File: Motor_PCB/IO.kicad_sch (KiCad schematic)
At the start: 54 parts, among them Q401 BC846, Q402 TPH4R50ANH1, Q403 TPH4R50ANH1, Q404 2N7002, Q405 2N7002, Q406 BC856, U401 VOM1271T, U402 TCAN1043xDxQ1

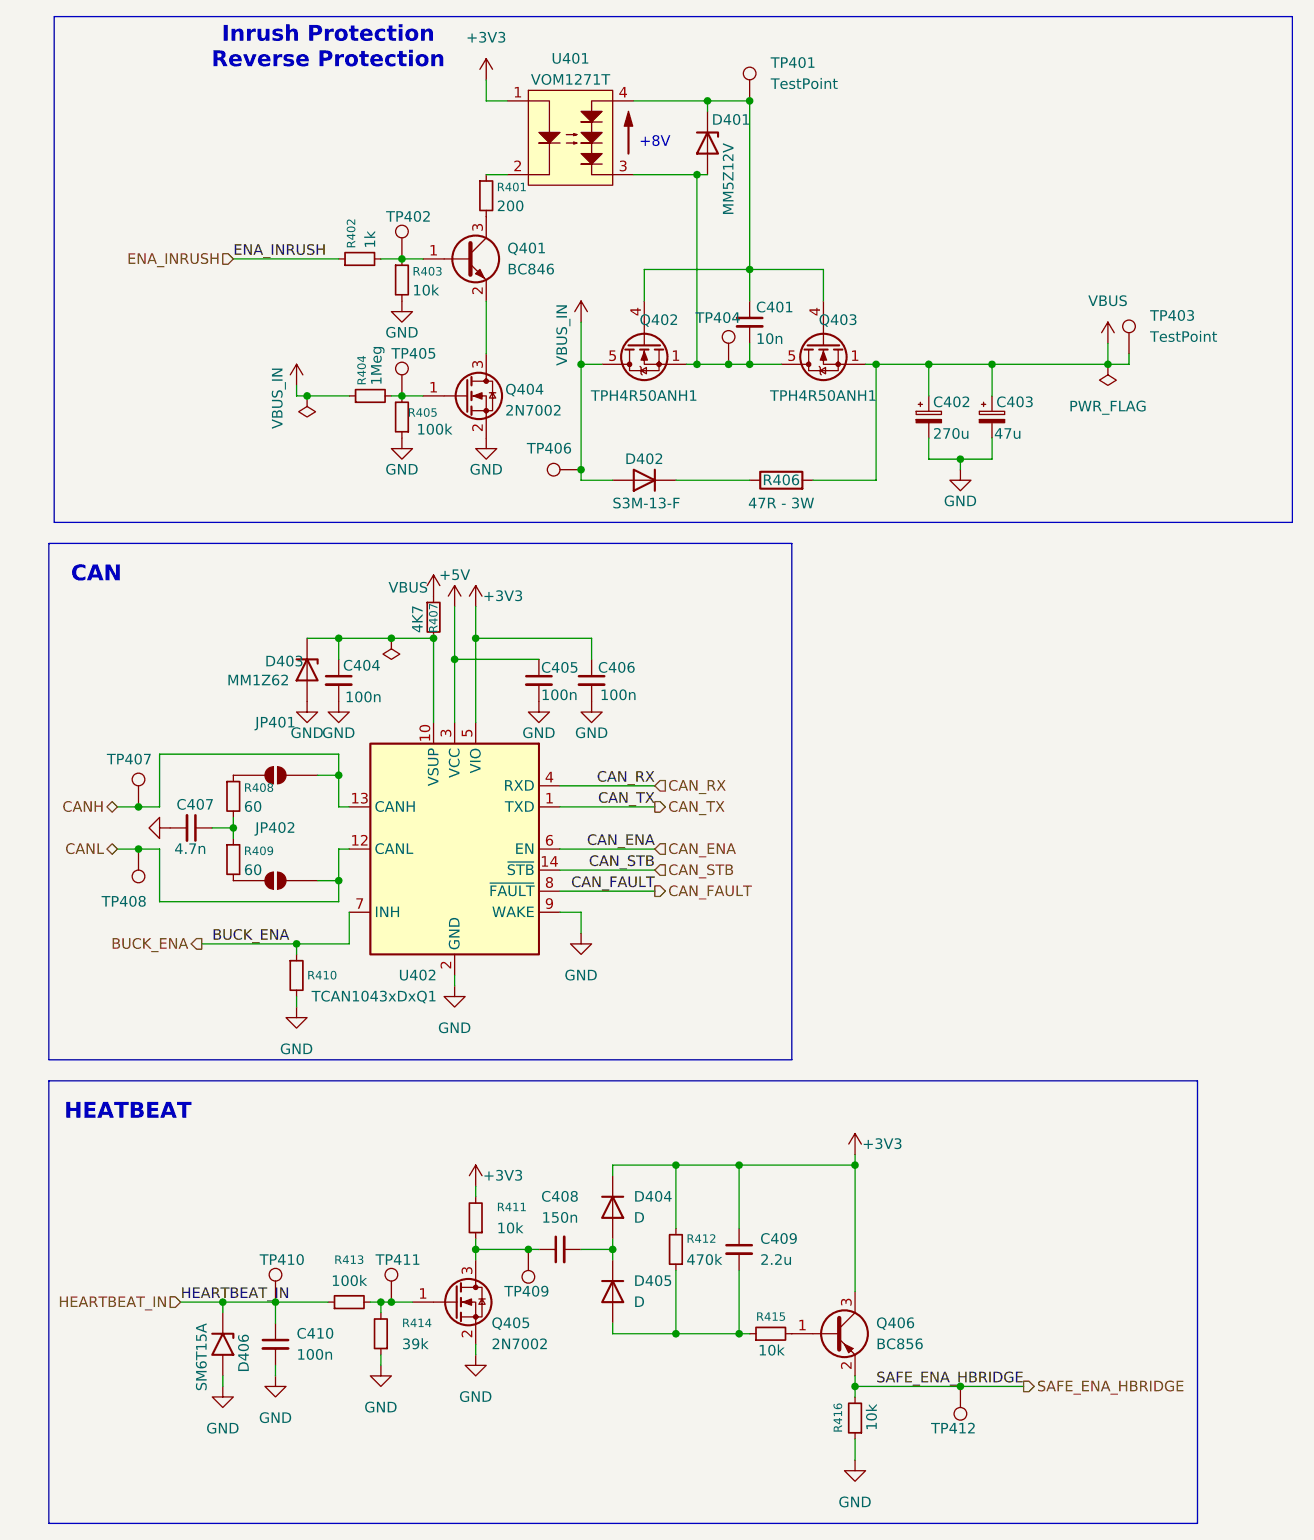
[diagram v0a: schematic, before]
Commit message: Fixed some Schematic mistakes
- Fixed mirroers FETS
- Added voltage divider to TCAN INH
- fixed other minor mistakes
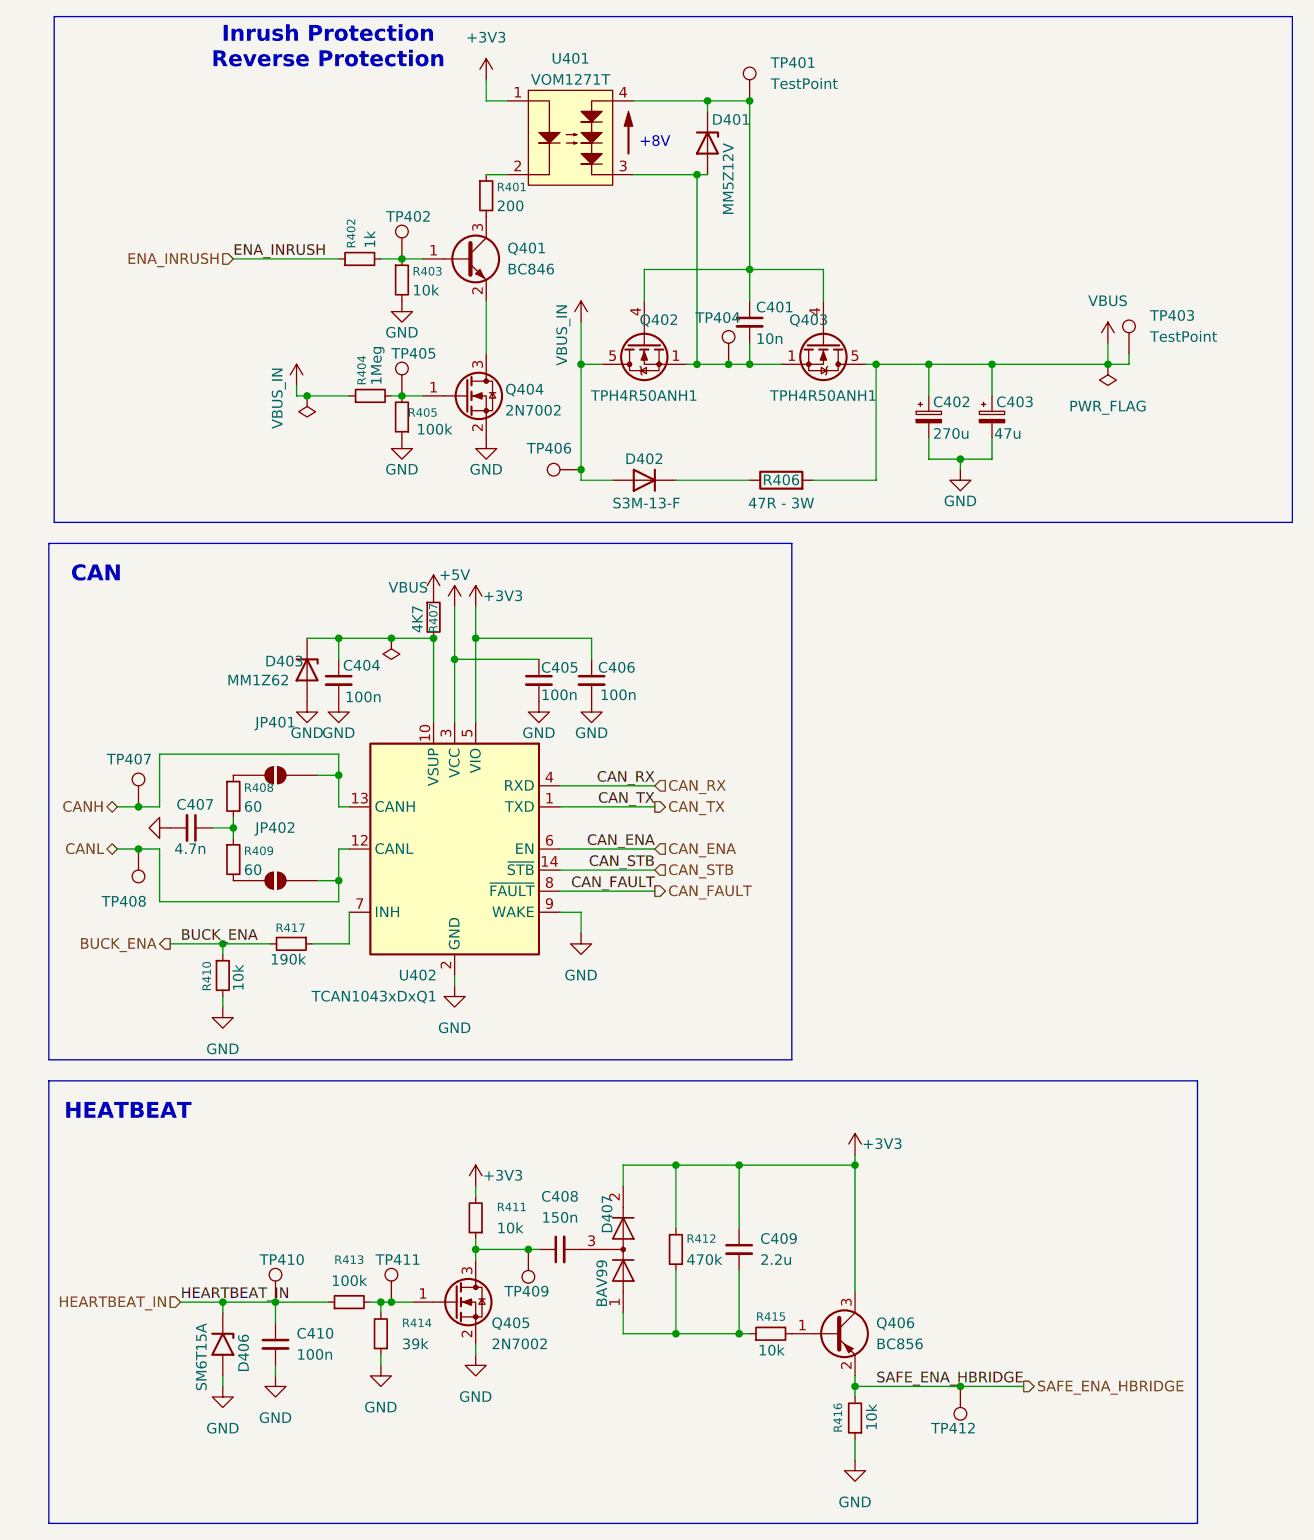
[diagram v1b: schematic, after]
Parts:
- removed D404, D405: D, Package_TO_SOT_SMD:SOT-23, symbol Device:D
- added D407: BAV99, Package_TO_SOT_SMD:SOT-23, symbol Diode:BAV99
- added R417: 190k, Resistor_SMD:R_0603_1608Metric, symbol Device:R_Small
- C408, C409, C410: footprint Diode_SMD:D_SMB -> Capacitor_SMD:C_0603_1608Metric
- D402: footprint Diode_SMD:D_SOD-323 -> Diode_SMD:D_SMC
- D403: footprint Diode_SMD:Littelfuse_PolyZen-LS -> Diode_SMD:D_SOD-123
- R407, R411, R412, R413, R414, R415, R416: footprint Resistor_THT:R_Array_SIP4 -> Resistor_SMD:R_0603_1608Metric
- R410: value 60 -> 10k
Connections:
- net +3V3: now also D407.2 (A)
- net BUCK_ENA: now also R417.2; no longer U402.7 (INH)
- net VBUS: now also Q403.5 (D); no longer Q403.1 (S), Q403.2 (S), Q403.3 (S)
- net at C409.2, R412.1, R415.1: now also D407.1 (K)
- net at C401.2, D401.2 (A), Q402.1 (S)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: now also Q403.1 (S), Q403.2 (S), Q403.3 (S); no longer Q403.5 (D)
- net at C408.2: now also D407.3 (K)
- new net: R417.1, U402.7 (INH)
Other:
- moved on the sheet: Q403, R410

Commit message: Surely i didnt miss anything else on the schematc...
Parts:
- R413: value 100k -> 50k
- R414: value 39k -> 100k
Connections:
- net +3V3: now also Q406.2 (E); no longer Q406.3 (C)
- net SAFE_ENA_HBRIDGE: now also Q406.3 (C); no longer Q406.2 (E)
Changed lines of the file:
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@@
 		(lib_id "Transistor_BJT:BC856")
 		(at 111.76 172.72 0)
+		(mirror x)
 		(unit 1)
 		(body_style 1)
@@
 		(in_pos_files yes)
 		(dnp no)
-		(fields_autoplaced yes)
 		(property "Reference" "Q406"
-			(at 116.84 171.4499 0)
+			(at 116.84 173.9901 0)
 			(show_name no)
 			(do_not_autoplace no)
@@
 		)
 		(property "Value" "BC856"
-			(at 116.84 173.9899 0)
+			(at 116.84 171.4501 0)
 			(show_name no)
 			(do_not_autoplace no)
@@
 		)
 		(property "Footprint" "Package_TO_SOT_SMD:SOT-23"
-			(at 116.84 174.625 0)
+			(at 116.84 170.815 0)
 			(hide yes)
 			(show_name no)
@@
 			)
 		)
-		(property "Value" "100k"
+		(property "Value" "50k"
 			(at 53.34 166.37 90)
 			(show_name no)
@@
 			)
 		)
-		(property "Value" "39k"
+		(property "Value" "100k"
 			(at 59.69 173.9899 0)
 			(show_name no)

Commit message: Updated schematic started on layout for motor PCB
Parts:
- removed TP407, TP408: TestPoint, TestPoint:TestPoint_Pad_D1.5mm, symbol Connector:TestPoint
- added C411: 100u, Capacitor_SMD:CP_Elec_10x10, symbol Device:C_Polarized_Small
- added D404: ESD2CANFD60-Q1, Package_TO_SOT_SMD:SOT-23-3, symbol Device:D_TVS_Dual_AAC
- C402: value 270u -> 100u; footprint Capacitor_SMD:CP_Elec_8x10.5 -> Capacitor_SMD:CP_Elec_10x10
- C403: value 47u -> 100u; footprint Capacitor_SMD:CP_Elec_8x10.5 -> Capacitor_SMD:CP_Elec_10x10
- U401: footprint Package_SO:SOP-4_7.5x4.1mm_P2.54mm -> MOTOR_PCB:SOP-4_VIS
- U402: value TCAN1043xDxQ1 -> TCAN1043H
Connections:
- net CANH: now also D404.2 (A2)
- net CANL: now also D404.1 (A1)
- net GND: now also C411.2, D404.3 (common)
- net VBUS: now also C411.1
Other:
- moved on the sheet: C404, C405, C406, C407, D403, JP401, JP402, R407, R408, R409, R410, R417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

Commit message: 20/10-2026
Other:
- moved on the sheet: C401, C402, C403, C404, C405, C406, C407, C408, C409, C410, C411, D401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

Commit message: 23-10-2026
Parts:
- Q404: value 2N7002 -> AO3400A; symbol Transistor_FET:2N7002 -> Transistor_FET:AO3400A
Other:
- note added: "Look at layout on CBT1 (placement, GND, distance from mcu and connector)"
- note added: "Reverse voltage of diode"
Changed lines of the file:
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@@
+		)
+	)
+	(text "Reverse voltage of diode"
+		(exclude_from_sim no)
+		(at 83.82 73.66 0)
+		(effects
+			(font
+				(size 1.27 1.27)
+			)
 		)
 	)
@@
 		)
 	)
+	(text "Look at layout on CBT1\n(placement, GND, distance from mcu and connector)"
+		(exclude_from_sim no)
+		(at 74.93 102.87 0)
+		(effects
+			(font
+				(size 1.27 1.27)
+			)
+		)
+	)
 	(text "CAN"
 		(exclude_from_sim no)
@@
 	(text "Inrush Protection\nReverse Protection"
 		(exclude_from_sim no)
-		(at 48.26 17.78 0)
+		(at 31.75 19.05 0)
 		(effects
 			(font
@@
 	)
 	(symbol
-		(lib_id "Transistor_FET:2N7002")
+		(lib_id "Transistor_FET:AO3400A")
 		(at 64.77 59.69 0)
 		(unit 1)
@@
 			)
 		)
-		(property "Value" "2N7002"
+		(property "Value" "AO3400A"
 			(at 69.596 61.468 0)
 			(show_name no)
@@
 			)
 		)
-		(property "Datasheet" "https://www.onsemi.com/pub/Collateral/NDS7002A-D.PDF"
+		(property "Datasheet" "http://www.aosmd.com/pdfs/datasheet/AO3400A.pdf"
 			(at 69.85 63.5 0)
 			(hide yes)
@@
 			)
 		)
-		(property "Description" "0.115A Id, 60V Vds, N-Channel MOSFET, SOT-23"
+		(property "Description" "30V Vds, 5.7A Id, N-Channel MOSFET, SOT-23"
 			(at 64.77 59.69 0)
 			(hide yes)
